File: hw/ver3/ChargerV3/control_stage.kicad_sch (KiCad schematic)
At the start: 5 parts, among them J5 FanConnector, J6 Conn_02x07_Odd_Even

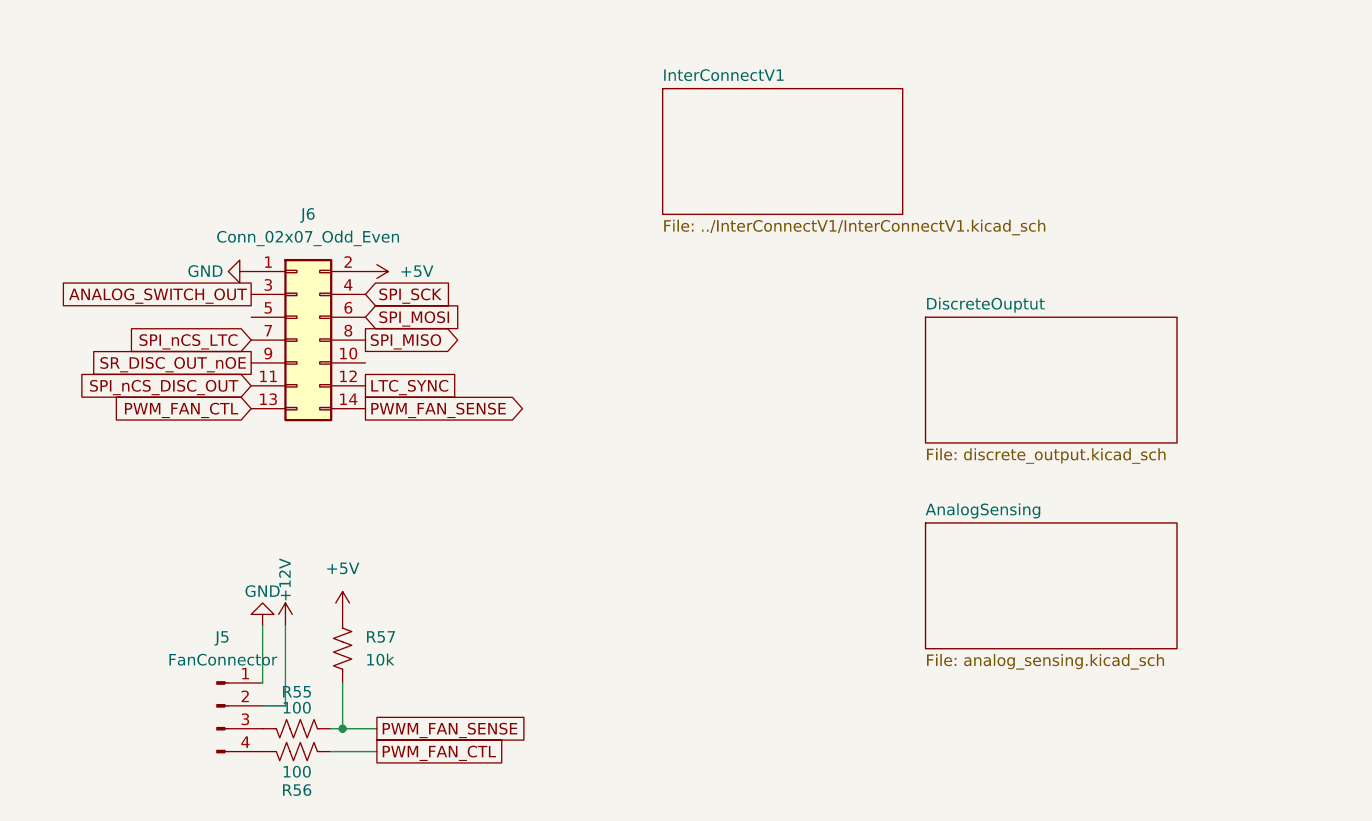
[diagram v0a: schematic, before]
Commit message: Redo some charger routing. Improve design for interconnect
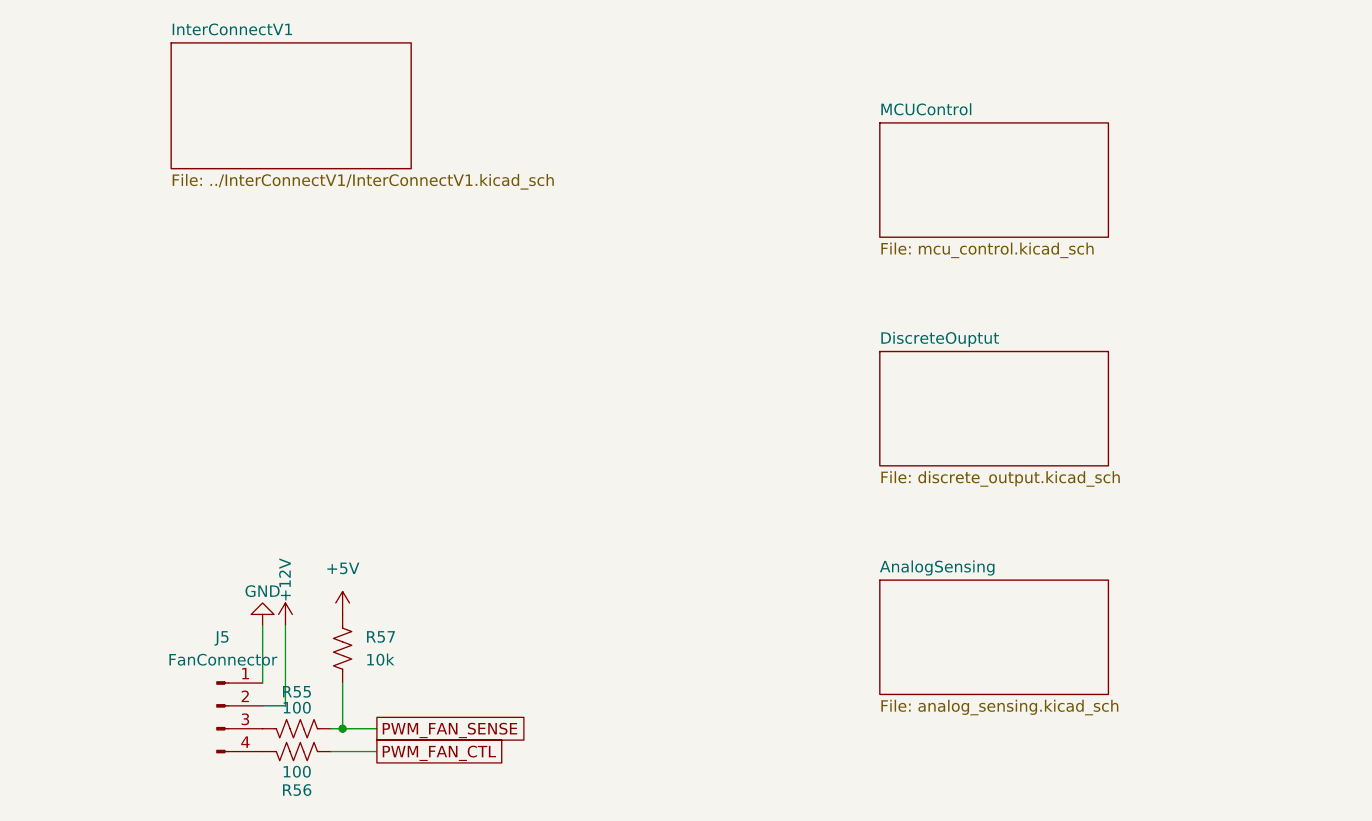
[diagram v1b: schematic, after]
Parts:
- removed J6: Conn_02x07_Odd_Even, Connector_IDC:IDC-Header_2x07_P2.54mm_Vertical, symbol Connector_Generic:Conn_02x07_Odd_Even
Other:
- added sheet MCUControl (mcu_control.kicad_sch)

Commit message: Nearly final charger schematic, updated with RS485 interconnect.
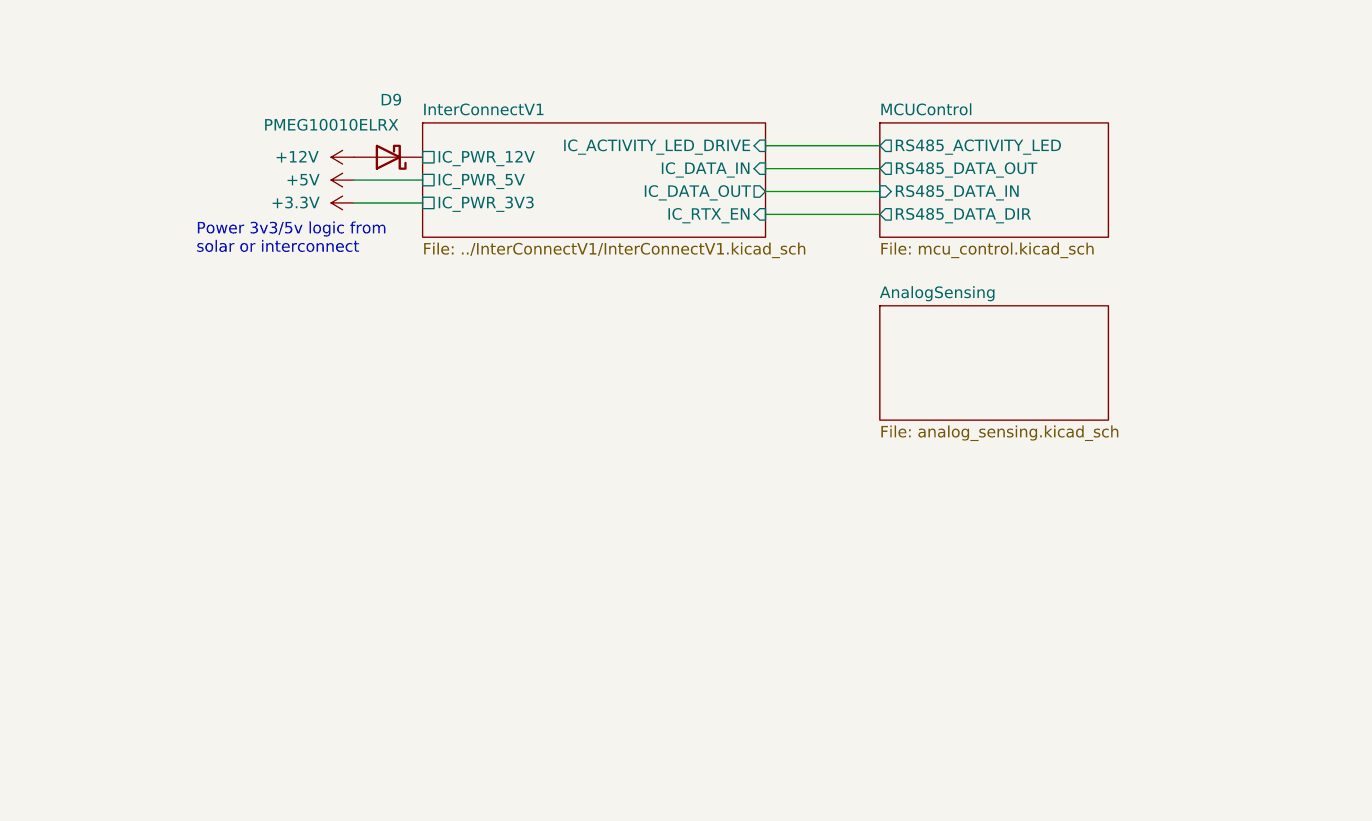
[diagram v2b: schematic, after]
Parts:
- removed J5: FanConnector, Connector_Molex:Molex_KK-254_AE-6410-04A_1x04_P2.54mm_Vertical, symbol Connector:Conn_01x04_Pin
- removed R55, R56: 100, Resistor_SMD:R_0603_1608Metric, symbol Device:R_US
- removed R57: 10k, Resistor_SMD:R_0603_1608Metric, symbol Device:R_US
- added D9: PMEG10010ELRX, Diode_SMD:D_SOD-123, symbol Device:D_Schottky
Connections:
- net +12V: now also D9.2 (A)
- new net InterConnectV1/IC_PWR_12V: D9.1 (K)
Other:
- removed sheet DiscreteOuptut
- sheet InterConnectV1 ports: added IC_ACTIVITY_LED_DRIVE, IC_DATA_IN, IC_DATA_OUT, IC_PWR_12V, IC_PWR_3V3, IC_PWR_5V, IC_RTX_EN; removed none
- sheet MCUControl ports: added RS485_ACTIVITY_LED, RS485_DATA_DIR, RS485_DATA_IN, RS485_DATA_OUT; removed none
- note added: "Power 3v3/5v logic from solar or interconnect"

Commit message: Sync board changes from before work started
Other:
- sheet InterConnectV1 ports: added IC_LED_IN_G, IC_LED_IN_Y, IC_LED_OUT_G, IC_LED_OUT_Y; removed IC_ACTIVITY_LED_DRIVE
- sheet MCUControl ports: added RS485_LINK_STATE; removed RS485_ACTIVITY_LED
- moved on the sheet: D9
